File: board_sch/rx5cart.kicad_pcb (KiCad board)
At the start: 2 copper layers, 140.7 x 101.8 mm, 9 parts, among them P1 RX5_WDC, U1 TEENSYPP2, U2 TC551001, U3 TC551001

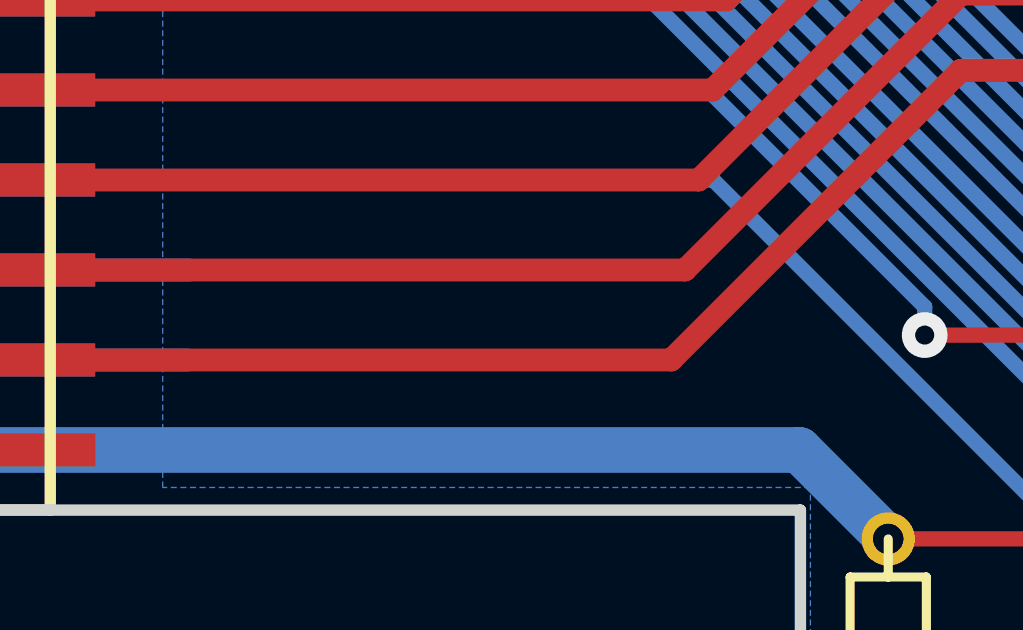
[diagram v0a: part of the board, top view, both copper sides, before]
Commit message: Change ground plane
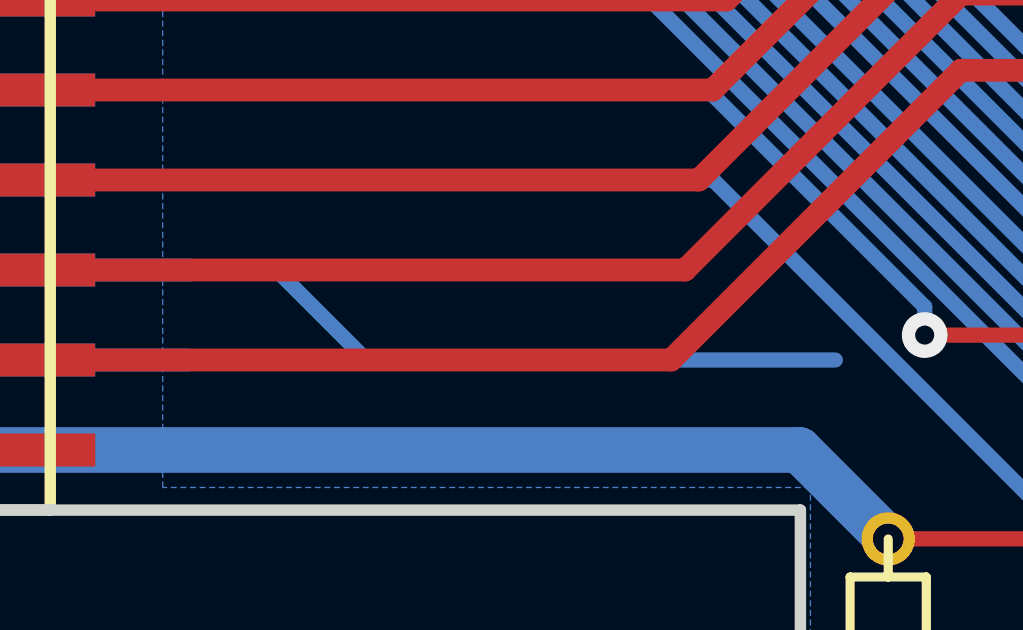
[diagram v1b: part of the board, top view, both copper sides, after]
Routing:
- net GND: track 111.2 -> 139.9 mm
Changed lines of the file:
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@@
     (thickness 1.6002)
     (drawings 15)
-    (tracks 798)
+    (tracks 802)
     (zones 0)
     (modules 9)
@@
     (33 F.Adhes user hide)
     (35 F.Paste user hide)
-    (37 F.SilkS user hide)
+    (37 F.SilkS user)
     (38 B.Mask user hide)
-    (39 F.Mask user hide)
+    (39 F.Mask user)
     (40 Dwgs.User user hide)
     (41 Cmts.User user hide)
@@
       (usegerberattributes false)
       (usegerberadvancedattributes false)
-      (creategerberjobfile true)
+      (creategerberjobfile false)
       (excludeedgelayer true)
       (linewidth 0.150000)
@@
       (psa4output false)
       (plotreference true)
-      (plotvalue false)
+      (plotvalue true)
       (plotinvisibletext false)
       (padsonsilk false)
@@
     (add_net "Net-(D1-Pad1)")
     (add_net "Net-(D2-Pad1)")
+    (add_net "Net-(P1-PadPROT)")
+    (add_net "Net-(U1-Pad11)")
+    (add_net "Net-(U1-Pad12)")
+    (add_net "Net-(U1-Pad2)")
+    (add_net "Net-(U1-Pad41)")
+    (add_net "Net-(U1-Pad44)")
+    (add_net "Net-(U1-Pad46)")
+    (add_net "Net-(U1-Pad51)")
     (add_net VCC)
   )
@@
       (effects (font (size 0.762 0.762) (thickness 0.0889)))
     )
+    (fp_line (start 1.8288 1.27) (end 1.8288 -1.27) (layer F.SilkS) (width 0.254))
     (fp_arc (start 0.254 0) (end -1.27 0) (angle 39.8) (layer F.SilkS) (width 0.1524))
     (fp_arc (start 0.254 0) (end -0.88392 1.01092) (angle 41.6) (layer F.SilkS) (width 0.1524))
@@
     (fp_arc (start 0.254 0) (end -1.778 0) (angle 28.3) (layer F.SilkS) (width 0.254))
     (fp_arc (start 0.254 0) (end -1.47574 1.06426) (angle 31.6) (layer F.SilkS) (width 0.254))
-    (fp_line (start 1.8288 1.27) (end 1.8288 -1.27) (layer F.SilkS) (width 0.254))
     (pad 1 thru_hole circle (at -1.27 0 90) (size 1.6764 1.6764) (drill 0.8128) (layers *.Cu *.Mask F.SilkS)
       (net 29 "Net-(D2-Pad1)"))
@@
   (segment (start 131.496001 82.5666) (end 135.490041 86.56064) (width 0.508) (layer B.Cu) (net 25))
   (segment (start 39.5097 104.97058) (end 49.09058 104.97058) (width 0.762) (layer B.Cu) (net 26))
-  (segment (start 39.5097 101.97084) (end 49.15916 101.97084) (width 0.762) (layer B.Cu) (net 26))
   (segment (start 39.5097 59.9694) (end 50.5206 59.9694) (width 1.524) (layer B.Cu) (net 26))
   (via (at 109.22 66.04) (size 1.524) (drill 0.635) (layers F.Cu B.Cu) (net 26))
@@
   (segment (start 95.25 107.95) (end 95.25 107.95) (width 0.508) (layer F.Cu) (net 26))
   (via (at 95.25 107.95) (size 1.524) (drill 0.635) (layers F.Cu B.Cu) (net 26))
+  (segment (start 39.5097 101.97084) (end 49.15916 101.97084) (width 0.762) (layer B.Cu) (net 26))
+  (segment (start 52.04968 101.97084) (end 55.04942 104.97058) (width 0.508) (layer B.Cu) (net 26))
+  (segment (start 49.15916 101.97084) (end 52.04968 101.97084) (width 0.508) (layer B.Cu) (net 26))
+  (segment (start 55.04942 104.97058) (end 70.68058 104.97058) (width 0.508) (layer B.Cu) (net 26))
+  (segment (start 49.09058 104.97058) (end 55.04942 104.97058) (width 0.508) (layer B.Cu) (net 26))
   (segment (start 121.165467 38.353971) (end 124.746505 38.353971) (width 0.508) (layer F.Cu) (net 27))
   (segment (start 106.179438 53.34) (end 121.165467 38.353971) (width 0.508) (layer F.Cu) (net 27))
@@
       )
     )
+  )
+  (zone (net 0) (net_name "") (layer B.Cu) (hatch edge 0.508)
+    (connect_pads (clearance 0.508))
+    (min_thickness 0.254)
+    (keepout (tracks allowed) (vias allowed) (copperpour not_allowed))
+    (fill (arc_segments 32) (thermal_gap 0.508) (thermal_bridge_width 0.508))
+    (polygon
+      (pts
+        (xy 69.85 106.68) (xy 48.26 106.68) (xy 48.26 99.06) (xy 69.85 99.06)
+      )
+    )

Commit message: Unfinished PCB
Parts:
- added R2: 10k, rx5cart_footprints:RESISTOR, F.Cu at (102.9, 115.6)
- added R3: 10k, rx5cart_footprints:RESISTOR, F.Cu at (102.9, 112.2)
